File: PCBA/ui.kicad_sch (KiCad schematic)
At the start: 4 parts, among them SW801 SW_Push, SW802 SW_Push, SW803 SW_Push, SW804 SW_Push

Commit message: LCD
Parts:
- added J701: FH12-24S-0.5SH(55), Connector_FFC-FPC:Hirose_FH12-24S-0.5SH_1x24-1MP_P0.50mm_Horizontal, symbol Connector_Generic_MountingPin:Conn_01x24_MountingPin
- added Q?: 2N7002, Package_TO_SOT_SMD:SOT-23, symbol Transistor_FET:2N7002
- added R?: 200?, symbol Device:R
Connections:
- net LCD Backlight: now also Q?.1 (G)
- net LCD COPI: now also J701.12 (Pin_12)
- net LCD DC: now also J701.10 (Pin_10)
- net LCD SCK: now also J701.9 (Pin_9)
- net VDD: now also J701.4 (Pin_4), J701.5 (Pin_5), J701.6 (Pin_6), R?.1
- net ~{LCD CS}: now also J701.8 (Pin_8)
- new net: J701.1 (Pin_1), R?.2
- new net: J701.2 (Pin_2), Q?.3 (D)
- new net GND: J701.11 (Pin_11), J701.13 (Pin_13), J701.14 (Pin_14), J701.15 (Pin_15), J701.16 (Pin_16), J701.17 (Pin_17), J701.18 (Pin_18), J701.19 (Pin_19), J701.20 (Pin_20), J701.23 (Pin_23), J701.24 (Pin_24), J701.3 (Pin_3), J701.MP (MountPin), Q?.2 (S)
- new net TE (not used): J701.21 (Pin_21)
- new net ~{LCD Reset}: J701.7 (Pin_7)
- no-connect marks 0 -> 1
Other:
- note added: "LEDA LEDK GND VDD (2.8V-3.3V) VDDIO (3.3V) IM1/2 RESET CS D/C WR RD SDA DB0 DB1 DB2 DB3 DB4 DB5 DB6 DB7 TE (hsync) NC GND GND"
- note added: "Not sure correct value, needs testing"
- note added: "Sets to spi mode"

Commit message: Add link to screen
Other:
- note added: "IPS 1.3 inch 24PIN SPI Color TFT Display Screen ST7789 Drive IC 3.3V 8Bit Parallel Interface 240*240"
- note added: "https://www.aliexpress.com/item/1924508571.html"
- note added: "https://www.aliexpress.com/item/33047794662.html"
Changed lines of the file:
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@@
+    (effects (font (size 1.27 1.27)) (justify left bottom))
+  )
+  (text "https://www.aliexpress.com/item/1924508571.html" (at 133.35 132.08 0)
     (effects (font (size 1.27 1.27)) (justify left bottom))
   )
@@
     (effects (font (size 1.27 1.27)) (justify left bottom))
   )
+  (text "https://www.aliexpress.com/item/33047794662.html" (at 132.08 129.54 0)
+    (effects (font (size 1.27 1.27)) (justify left bottom))
+  )
+  (text "IPS 1.3 inch 24PIN SPI Color TFT Display Screen ST7789 Drive IC 3.3V 8Bit Parallel Interface 240*240"
+    (at 116.84 125.73 0)
+    (effects (font (size 1.27 1.27)) (justify left bottom))
+  )

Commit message: Add Qwiic
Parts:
- gave numbers to parts that had none: 2
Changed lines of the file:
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@@
   (symbol (lib_id "Transistor_FET:2N7002") (at 111.76 81.28 0) (unit 1)
     (in_bom yes) (on_board yes) (fields_autoplaced)
-    (property "Reference" "Q?" (id 0) (at 118.11 80.0099 0)
+    (property "Reference" "Q701" (id 0) (at 118.11 80.0099 0)
       (effects (font (size 1.27 1.27)) (justify left))
     )
@@
   (symbol (lib_id "power:GND") (at 114.3 86.36 0) (unit 1)
     (in_bom yes) (on_board yes) (fields_autoplaced)
-    (property "Reference" "#PWR?" (id 0) (at 114.3 92.71 0)
+    (property "Reference" "#PWR0149" (id 0) (at 114.3 92.71 0)
       (effects (font (size 1.27 1.27)) hide)
     )
@@
   (symbol (lib_id "Device:R") (at 177.8 29.21 0) (unit 1)
     (in_bom yes) (on_board yes) (fields_autoplaced)
-    (property "Reference" "R?" (id 0) (at 180.34 27.9399 0)
+    (property "Reference" "R705" (id 0) (at 180.34 27.9399 0)
       (effects (font (size 1.27 1.27)) (justify left))
     )
@@
   (symbol (lib_id "power:VDD") (at 177.8 25.4 0) (unit 1)
     (in_bom yes) (on_board yes) (fields_autoplaced)
-    (property "Reference" "#PWR?" (id 0) (at 177.8 29.21 0)
+    (property "Reference" "#PWR0148" (id 0) (at 177.8 29.21 0)
       (effects (font (size 1.27 1.27)) hide)
     )
@@
   (symbol (lib_id "power:GND") (at 195.58 114.3 0) (unit 1)
     (in_bom yes) (on_board yes) (fields_autoplaced)
-    (property "Reference" "#PWR?" (id 0) (at 195.58 120.65 0)
+    (property "Reference" "#PWR0151" (id 0) (at 195.58 120.65 0)
       (effects (font (size 1.27 1.27)) hide)
     )
@@
   (symbol (lib_id "power:GND") (at 187.96 116.84 0) (unit 1)
     (in_bom yes) (on_board yes) (fields_autoplaced)
-    (property "Reference" "#PWR?" (id 0) (at 187.96 123.19 0)
+    (property "Reference" "#PWR0150" (id 0) (at 187.96 123.19 0)
       (effects (font (size 1.27 1.27)) hide)
     )

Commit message: Assign footprints
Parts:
- R705: footprint (none) -> Resistor_SMD:R_0603_1608Metric
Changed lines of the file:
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@@
       (effects (font (size 1.27 1.27)) (justify left))
     )
-    (property "Footprint" "" (id 2) (at 176.022 29.21 90)
+    (property "Footprint" "Resistor_SMD:R_0603_1608Metric" (id 2) (at 176.022 29.21 90)
       (effects (font (size 1.27 1.27)) hide)
     )

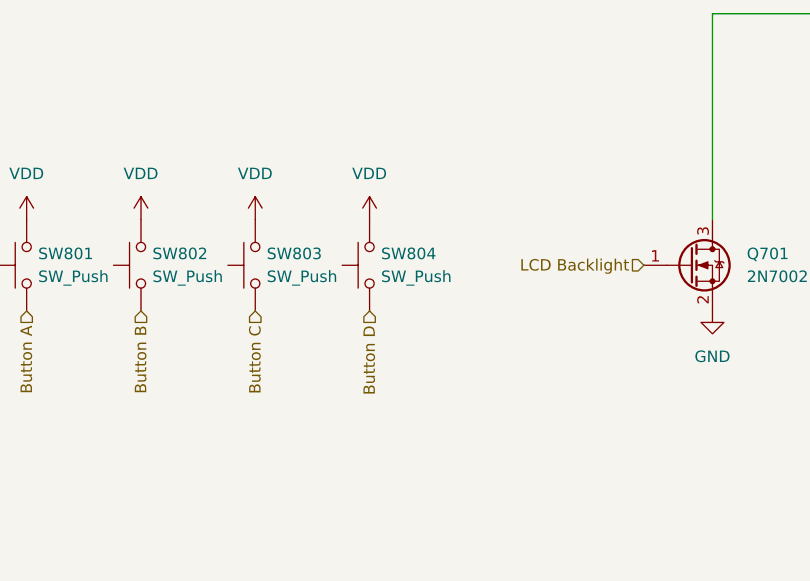
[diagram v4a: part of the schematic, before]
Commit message: Update schematic pinmap bl706
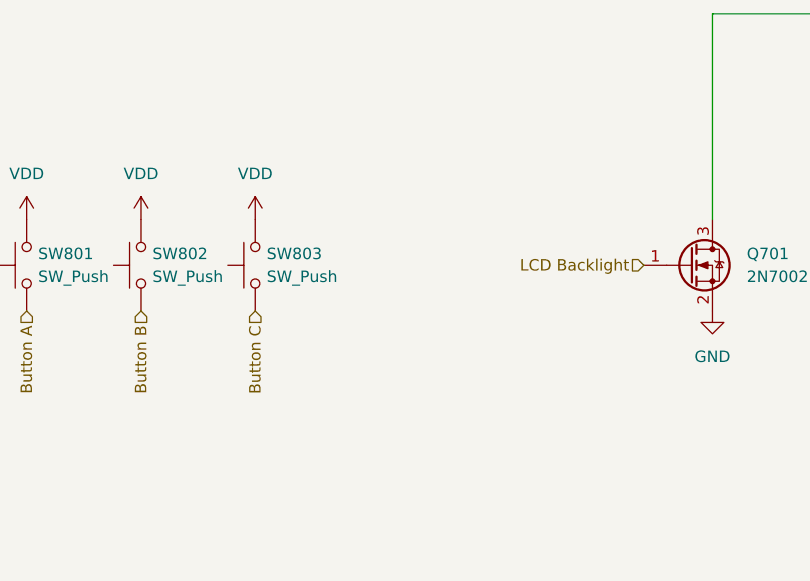
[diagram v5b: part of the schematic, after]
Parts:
- removed SW804: SW_Push, Button_Switch_THT:SW_Tactile_SKHH_Angled, symbol Switch:SW_Push
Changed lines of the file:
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@@
-    (effects (font (size 1.27 1.27)) (justify right))
-  )
-  (hierarchical_label "Button D" (shape input) (at 76.2 86.36 270)
     (effects (font (size 1.27 1.27)) (justify right))
   )
@@
     (pin "3")
   )
-  (symbol (lib_id "power:VDD") (at 76.2 76.2 0) (unit 1)
-    (in_bom yes) (on_board yes) (fields_autoplaced)
-    (property "Reference" "#PWR0146" (id 0) (at 76.2 80.01 0)
-      (effects (font (size 1.27 1.27)) hide)
-    )
-    (property "Value" "VDD" (id 1) (at 76.2 71.12 0))
-    (property "Footprint" "" (id 2) (at 76.2 76.2 0)
-      (effects (font (size 1.27 1.27)) hide)
-    )
-    (property "Datasheet" "" (id 3) (at 76.2 76.2 0)
-      (effects (font (size 1.27 1.27)) hide)
-    )
-    (pin "1")
-  )
   (symbol (lib_id "power:GND") (at 114.3 86.36 0) (unit 1)
     (in_bom yes) (on_board yes) (fields_autoplaced)
@@
     (pin "1")
   )
-  (symbol (lib_id "Switch:SW_Push") (at 76.2 81.28 90) (unit 1)
-    (in_bom yes) (on_board yes) (fields_autoplaced)
-    (property "Reference" "SW804" (id 0) (at 77.47 80.0099 90)
-      (effects (font (size 1.27 1.27)) (justify right))
-    )
-    (property "Value" "SW_Push" (id 1) (at 77.47 82.5499 90)
-      (effects (font (size 1.27 1.27)) (justify right))
-    )
-    (property "Footprint" "Button_Switch_THT:SW_Tactile_SKHH_Angled" (id 2) (at 71.12 81.28 0)
-      (effects (font (size 1.27 1.27)) hide)
-    )
-    (property "Datasheet" "~" (id 3) (at 71.12 81.28 0)
-      (effects (font (size 1.27 1.27)) hide)
-    )
-    (pin "1")
-    (pin "2")
-  )
   (symbol (lib_id "power:VDD") (at 38.1 76.2 0) (unit 1)

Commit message: Rough outline
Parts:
- removed J701: FH12-24S-0.5SH(55), Connector_FFC-FPC:Hirose_FH12-24S-0.5SH_1x24-1MP_P0.50mm_Horizontal, symbol Connector_Generic_MountingPin:Conn_01x24_MountingPin
- removed R705: 200?, Resistor_SMD:R_0603_1608Metric, symbol Device:R
- added C907: C, Capacitor_SMD:C_0603_1608Metric, symbol Device:C
- added C908, C909, C910: 0.1u, Capacitor_SMD:C_0603_1608Metric, symbol Device:C
- added C911: 1uf, Capacitor_SMD:C_0603_1608Metric, symbol Device:C
- added J901: Conn_02x25_Odd_Even_MountingPin, Connector_FFC-FPC:Molex_54132-5033_1x50-1MP_P0.5mm_Horizontal, symbol Connector_Generic_MountingPin:Conn_02x25_Odd_Even_MountingPin
- added R906, R907, R908, R909: 200?, Resistor_SMD:R_0603_1608Metric, symbol Device:R
- added U901: LP2985-2.8, Package_TO_SOT_SMD:SOT-23-5, symbol Regulator_Linear:LP2985-2.8
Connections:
- net GND: now also C907.2, C908.2, C909.2, C910.2, C911.2, J901.1 (Pin_1), J901.19 (Pin_19), J901.2 (Pin_2), J901.20 (Pin_20), J901.21 (Pin_21), J901.22 (Pin_22), J901.23 (Pin_23), J901.24 (Pin_24), J901.25 (Pin_25), J901.26 (Pin_26), J901.27 (Pin_27), J901.28 (Pin_28), J901.29 (Pin_29), J901.3 (Pin_3), J901.30 (Pin_30), J901.31 (Pin_31), J901.32 (Pin_32), J901.33 (Pin_33), J901.34 (Pin_34), J901.35 (Pin_35), J901.36 (Pin_36), J901.42 (Pin_42), J901.45 (Pin_45), J901.8 (Pin_8), U901.2 (GND)
- net LCD COPI: now also J901.17 (Pin_17)
- net LCD DC: now also J901.15 (Pin_15)
- net LCD SCK: now also J901.14 (Pin_14)
- net VDD: now also J901.16 (Pin_16), J901.43 (Pin_43), J901.44 (Pin_44), J901.50 (Pin_50), U901.1 (VIN), U901.3 (ON/~{OFF})
- net ~{LCD CS}: now also J901.13 (Pin_13)
- net ~{LCD Reset}: now also J901.4 (Pin_4), J901.41 (Pin_41)
- net LEDK: now reaches Q701.3 (D)
- net LEDK: now also R906.2, R907.1, R908.2, R909.1
- new net: J901.48 (Pin_48), R907.2
- new net: C907.1, U901.4 (BP)
- new net: J901.46 (Pin_46), R909.2
- new net: J901.47 (Pin_47), R908.1
- new net: J901.49 (Pin_49), R906.1
- new net INT: J901.5 (Pin_5)
- new net SCL: J901.7 (Pin_7)
- new net SDA: J901.6 (Pin_6)
- new net TE: J901.12 (Pin_12)
- new net VDD2.8: C908.1, C909.1, C910.1, C911.1, J901.10 (Pin_10), J901.11 (Pin_11), J901.9 (Pin_9), U901.5 (VOUT)
- no-connect marks 1 -> 5
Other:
- note added: "For SPI 4 wire mode: IM3 0 IM2 1 IM1 1 IM0 0"
- note added: "https://www.buydisplay.com/2-4-inch-ips-240x320-tft-lcd-display-capacitive-touch-screen"
- note added: "https://www.buydisplay.com/download/manual/ER-TFT024IPS-3_Datasheet.pdf"
- note removed: "IPS 1.3 inch 24PIN SPI Color TFT Display Screen ST7789 Drive IC 3.3V 8Bit Parallel Interface 240*240"
- note removed: "LEDA LEDK GND VDD (2.8V-3.3V) VDDIO (3.3V) IM1/2 RESET CS D/C WR RD SDA DB0 DB1 DB2 DB3 DB4 DB5 DB6 DB7 TE (hsync) NC GND GND"
- note removed: "Sets to spi mode"
- note removed: "https://www.aliexpress.com/item/1924508571.html"
- note removed: "https://www.aliexpress.com/item/33047794662.html"

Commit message: Routing
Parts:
- removed C910: 0.1u, Capacitor_SMD:C_0603_1608Metric, symbol Device:C
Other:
- moved on the sheet: C909
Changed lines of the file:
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@@
   (junction (at 190.5 96.52) (diameter 0) (color 0 0 0 0)
   )
-  (junction (at 207.01 151.13) (diameter 0) (color 0 0 0 0)
+  (junction (at 213.36 158.75) (diameter 0) (color 0 0 0 0)
   )
   (junction (at 190.5 78.74) (diameter 0) (color 0 0 0 0)
@@
   (junction (at 254 78.74) (diameter 0) (color 0 0 0 0)
   )
-  (junction (at 215.9 158.75) (diameter 0) (color 0 0 0 0)
-  )
-  (junction (at 207.01 158.75) (diameter 0) (color 0 0 0 0)
-  )
   (junction (at 254 81.28) (diameter 0) (color 0 0 0 0)
   )
@@
   (junction (at 254 76.2) (diameter 0) (color 0 0 0 0)
   )
+  (junction (at 213.36 151.13) (diameter 0) (color 0 0 0 0)
+  )
   (junction (at 254 83.82) (diameter 0) (color 0 0 0 0)
   )
@@
   )
   (junction (at 254 93.98) (diameter 0) (color 0 0 0 0)
-  )
-  (junction (at 215.9 151.13) (diameter 0) (color 0 0 0 0)
   )
   (junction (at 172.72 158.75) (diameter 0) (color 0 0 0 0)
@@
     (stroke (width 0) (type default) (color 0 0 0 0))
   )
+  (wire (pts (xy 213.36 151.13) (xy 226.06 151.13))
+    (stroke (width 0) (type default) (color 0 0 0 0))
+  )
   (wire (pts (xy 224.79 76.2) (xy 254 76.2))
     (stroke (width 0) (type default) (color 0 0 0 0))
@@
     (stroke (width 0) (type default) (color 0 0 0 0))
   )
+  (wire (pts (xy 213.36 158.75) (xy 226.06 158.75))
+    (stroke (width 0) (type default) (color 0 0 0 0))
+  )
   (wire (pts (xy 190.5 81.28) (xy 190.5 83.82))
     (stroke (width 0) (type default) (color 0 0 0 0))
@@
     (stroke (width 0) (type default) (color 0 0 0 0))
   )
-  (wire (pts (xy 215.9 158.75) (xy 226.06 158.75))
-    (stroke (width 0) (type default) (color 0 0 0 0))
-  )
   (wire (pts (xy 224.79 88.9) (xy 254 88.9))
     (stroke (width 0) (type default) (color 0 0 0 0))
@@
     (stroke (width 0) (type default) (color 0 0 0 0))
   )
-  (wire (pts (xy 198.12 151.13) (xy 207.01 151.13))
-    (stroke (width 0) (type default) (color 0 0 0 0))
-  )
   (wire (pts (xy 190.5 83.82) (xy 212.09 83.82))
     (stroke (width 0) (type default) (color 0 0 0 0))
@@
     (stroke (width 0) (type default) (color 0 0 0 0))
   )
-  (wire (pts (xy 215.9 151.13) (xy 226.06 151.13))
+  (wire (pts (xy 198.12 151.13) (xy 213.36 151.13))
     (stroke (width 0) (type default) (color 0 0 0 0))
   )
@@
     (stroke (width 0) (type default) (color 0 0 0 0))
   )
-  (wire (pts (xy 207.01 151.13) (xy 215.9 151.13))
-    (stroke (width 0) (type default) (color 0 0 0 0))
-  )
   (wire (pts (xy 190.5 76.2) (xy 190.5 78.74))
     (stroke (width 0) (type default) (color 0 0 0 0))
@@
     (stroke (width 0) (type default) (color 0 0 0 0))
   )
-  (wire (pts (xy 198.12 158.75) (xy 207.01 158.75))
+  (wire (pts (xy 198.12 158.75) (xy 213.36 158.75))
     (stroke (width 0) (type default) (color 0 0 0 0))
   )
@@
   )
   (wire (pts (xy 224.79 116.84) (xy 254 116.84))
-    (stroke (width 0) (type default) (color 0 0 0 0))
-  )
-  (wire (pts (xy 207.01 158.75) (xy 215.9 158.75))
     (stroke (width 0) (type default) (color 0 0 0 0))
   )
@@
     (pin "2")
   )
-  (symbol (lib_id "Device:C") (at 207.01 154.94 0) (unit 1)
+  (symbol (lib_id "Device:C") (at 213.36 154.94 0) (unit 1)
     (in_bom yes) (on_board yes) (fields_autoplaced)
-    (property "Reference" "C909" (id 0) (at 210.82 153.6699 0)
+    (property "Reference" "C909" (id 0) (at 217.17 153.6699 0)
       (effects (font (size 1.27 1.27)) (justify left))
     )
-    (property "Value" "0.1u" (id 1) (at 210.82 156.2099 0)
+    (property "Value" "0.1u" (id 1) (at 217.17 156.2099 0)
       (effects (font (size 1.27 1.27)) (justify left))
     )
-    (property "Footprint" "Capacitor_SMD:C_0603_1608Metric" (id 2) (at 207.9752 158.75 0)
-      (effects (font (size 1.27 1.27)) hide)
-    )
-    (property "Datasheet" "~" (id 3) (at 207.01 154.94 0)
+    (property "Footprint" "Capacitor_SMD:C_0603_1608Metric" (id 2) (at 214.3252 158.75 0)
+      (effects (font (size 1.27 1.27)) hide)
+    )
+    (property "Datasheet" "~" (id 3) (at 213.36 154.94 0)
       (effects (font (size 1.27 1.27)) hide)
     )
@@
       (effects (font (size 1.27 1.27)) hide)
     )
-    (pin "1")
-    (pin "2")
-  )
-  (symbol (lib_id "Device:C") (at 215.9 154.94 0) (unit 1)
-    (in_bom yes) (on_board yes) (fields_autoplaced)
-    (property "Reference" "C910" (id 0) (at 219.71 153.6699 0)
-      (effects (font (size 1.27 1.27)) (justify left))
-    )
-    (property "Value" "0.1u" (id 1) (at 219.71 156.2099 0)
-      (effects (font (size 1.27 1.27)) (justify left))
-    )
-    (property "Footprint" "Capacitor_SMD:C_0603_1608Metric" (id 2) (at 216.8652 158.75 0)
-      (effects (font (size 1.27 1.27)) hide)
-    )
-    (property "Datasheet" "~" (id 3) (at 215.9 154.94 0)
-      (effects (font (size 1.27 1.27)) hide)
-    )

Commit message: .
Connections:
- net Button A: now also SW803.1; no longer SW801.1
- net Button B: now also SW801.1; no longer SW802.1
- net Button C: now also SW802.1; no longer SW803.1
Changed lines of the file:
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@@
     (effects (font (size 1.27 1.27)) (justify right))
   )
-  (hierarchical_label "Button B" (shape input) (at 50.8 86.36 270)
+  (hierarchical_label "Button B" (shape input) (at 38.1 86.36 270)
     (effects (font (size 1.27 1.27)) (justify right))
   )
@@
     (effects (font (size 1.27 1.27)) (justify right))
   )
-  (hierarchical_label "Button C" (shape input) (at 63.5 86.36 270)
+  (hierarchical_label "Button C" (shape input) (at 50.8 86.36 270)
     (effects (font (size 1.27 1.27)) (justify right))
   )
-  (hierarchical_label "Button A" (shape input) (at 38.1 86.36 270)
+  (hierarchical_label "Button A" (shape input) (at 63.5 86.36 270)
     (effects (font (size 1.27 1.27)) (justify right))
   )
